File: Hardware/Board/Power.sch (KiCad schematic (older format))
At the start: 78 parts, among them Q100 2N7002, Q102 2N7002, Q103 2N7002, Q104 2N7002, U100 MAX17572, U101 MAX17572, U102 MAX17572, U104 MAX17574, U105 MAX17572

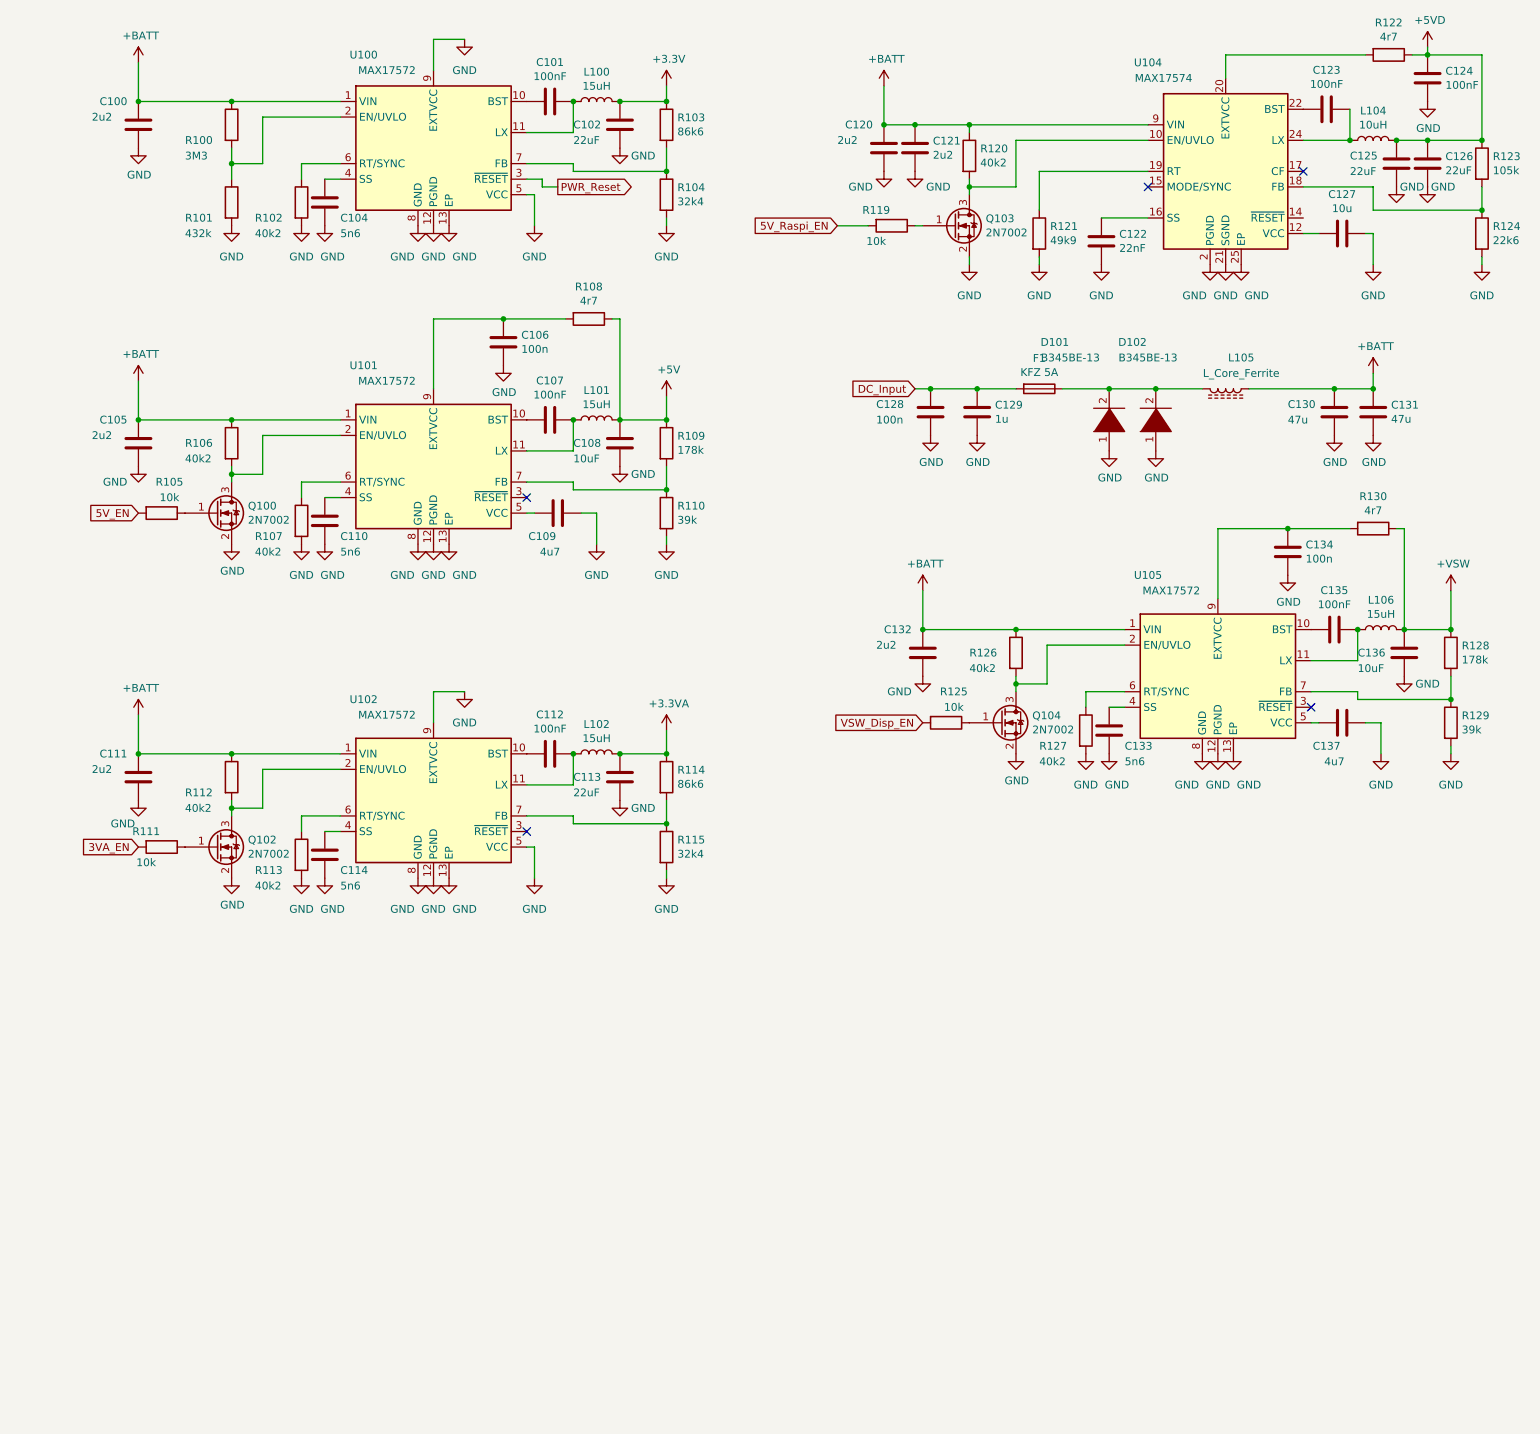
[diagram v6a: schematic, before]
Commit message: Display Unit Lib Fehler behoben, und noch Zeug raus geworfen Library jetzt projekt spezifisch im Hardware root.. Hauptplatine rund um den Prozessor a bissl was getan, vorbereitung Quadspi Flash und SD Karte.
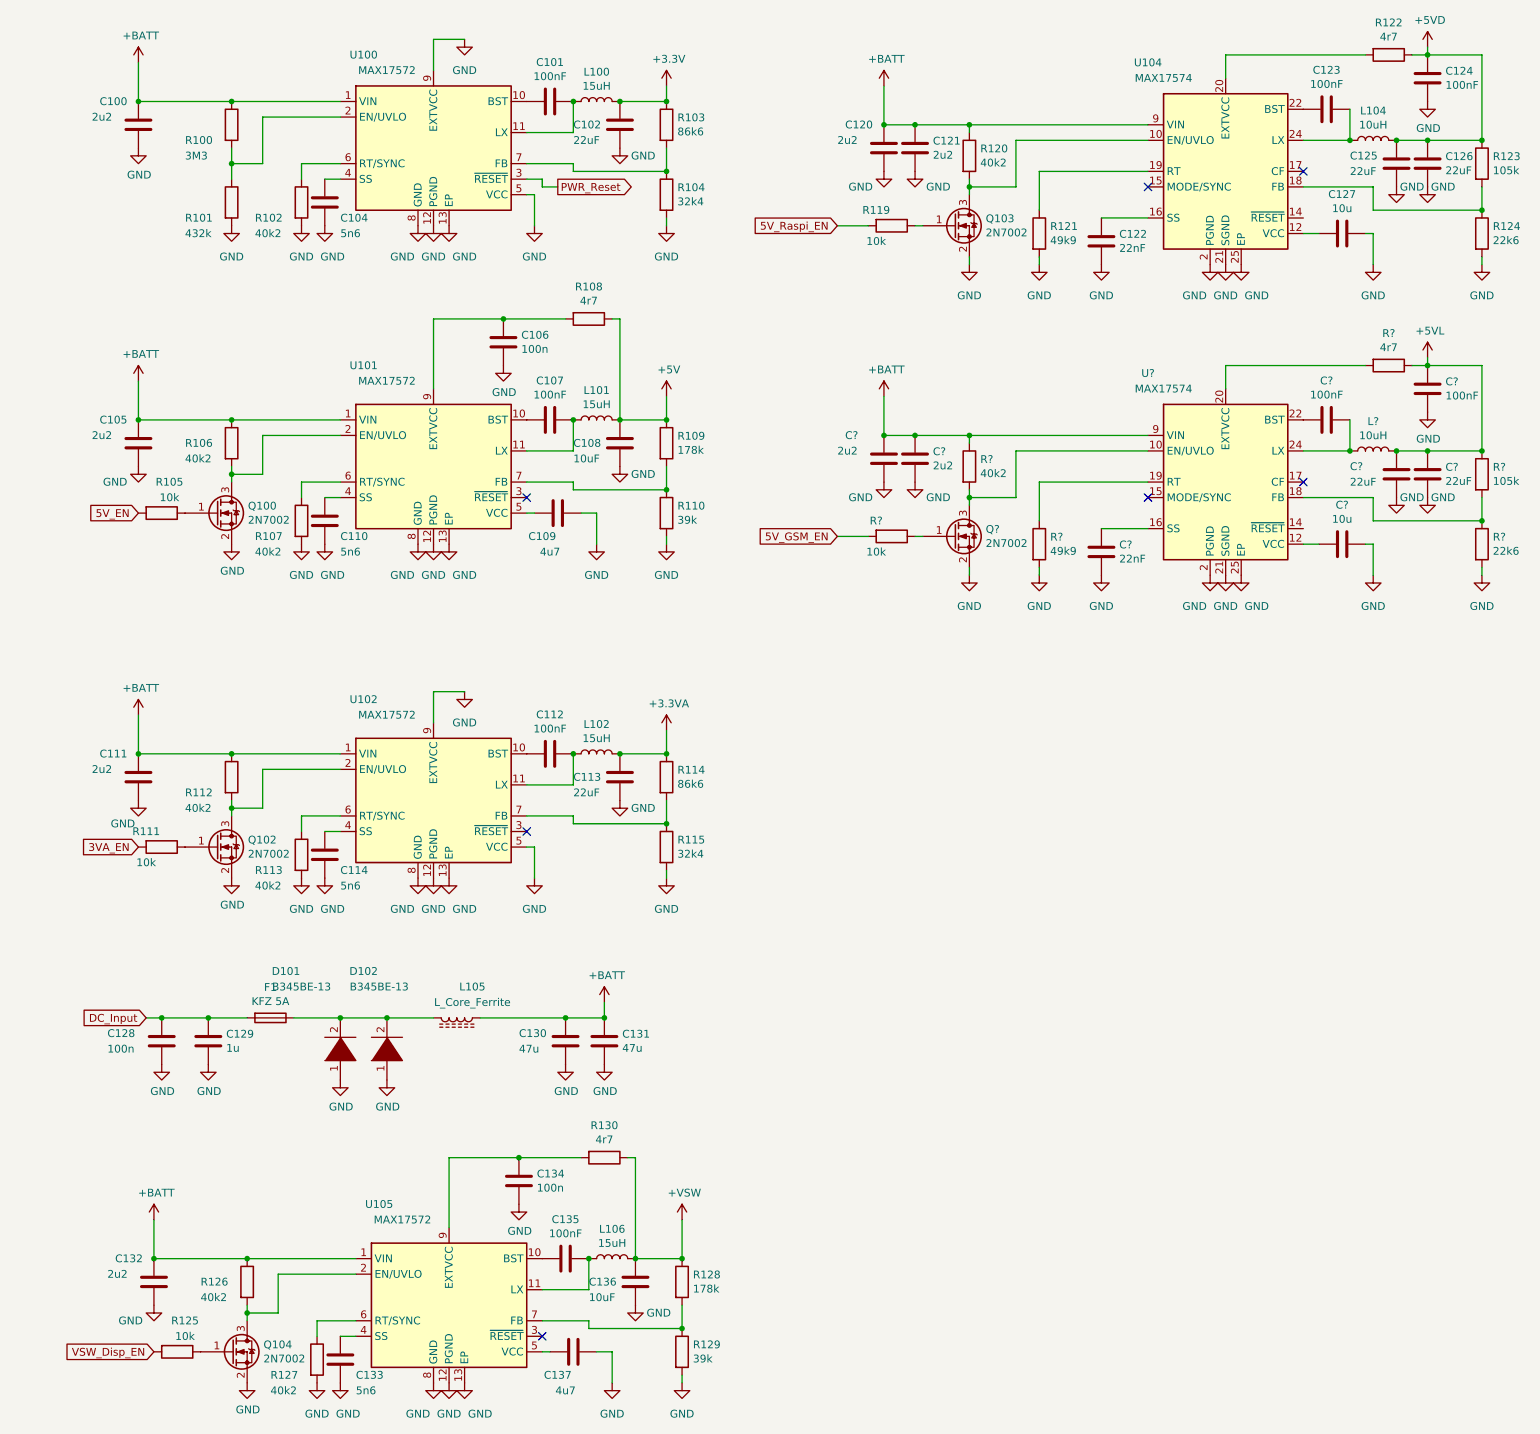
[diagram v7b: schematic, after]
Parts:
- added C?: 22nF, Capacitor_SMD:C_0603_1608Metric, symbol Device:C
- added C? (x2): 2u2, Capacitor_SMD:C_1210_3225Metric, symbol Device:C
- added C? (x2): 100nF, Capacitor_SMD:C_0603_1608Metric, symbol Device:C
- added C? (x2): 22uF, Capacitor_SMD:C_1210_3225Metric, symbol Device:C
- added C?: 10u, Capacitor_SMD:C_1210_3225Metric, symbol Device:C
- added L?: 10uH, SamacSys_Parts:XAL8080, symbol Device:L
- added Q?: 2N7002, Package_TO_SOT_SMD:SOT-23, symbol Transistor_FET:2N7002
- added R?: 105k, Resistor_SMD:R_0603_1608Metric, symbol Device:R
- added R?: 22k6, Resistor_SMD:R_0603_1608Metric, symbol Device:R
- added R?: 4r7, Resistor_SMD:R_0603_1608Metric, symbol Device:R
- added R?: 10k, Resistor_SMD:R_0603_1608Metric, symbol Device:R
- added R?: 40k2, Resistor_SMD:R_0603_1608Metric, symbol Device:R
- added R?: 49k9, Resistor_SMD:R_0603_1608Metric, symbol Device:R
- added U?: MAX17574, Package_DFN_QFN:QFN-24-1EP_4x5mm_P0.5mm_EP2.65x3.65mm, symbol Regulator_Switching:MAX17574
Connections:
- net +BATT: now also C?.1, C?.1, R?.1, U?.5 (VIN), U?.6 (VIN), U?.7 (VIN), U?.9 (VIN)
- net GND: now also C?.1, C?.2, C?.2, C?.2, C?.2, C?.2, C?.2, Q?.2 (S), R?.2, R?.2, U?.11 (PGND), U?.2 (PGND), U?.21 (SGND), U?.25 (EP), U?.3 (PGND)
- new net: C?.1, L?.1, U?.1 (LX), U?.23 (LX), U?.24 (LX)
- new net: Q?.3 (D), R?.2, U?.10 (EN/UVLO)
- new net: C?.2, U?.12 (VCC)
- new net: C?.1, U?.16 (SS)
- new net: R?.1, R?.2, U?.18 (FB)
- new net: R?.1, U?.19 (RT)
- new net: R?.2, U?.20 (EXTVCC)
- new net: C?.2, U?.22 (BST)
- new net: Q?.1 (G), R?.1
- new net +5VL: C?.1, C?.1, C?.1, L?.2, R?.1, R?.1
- new net 5V_GSM_EN: R?.2
- no-connect marks 5 -> 7
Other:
- moved on the sheet: C128, C129, C130, C131, C132, C133, C134, C135, C136, C137, D101, D102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

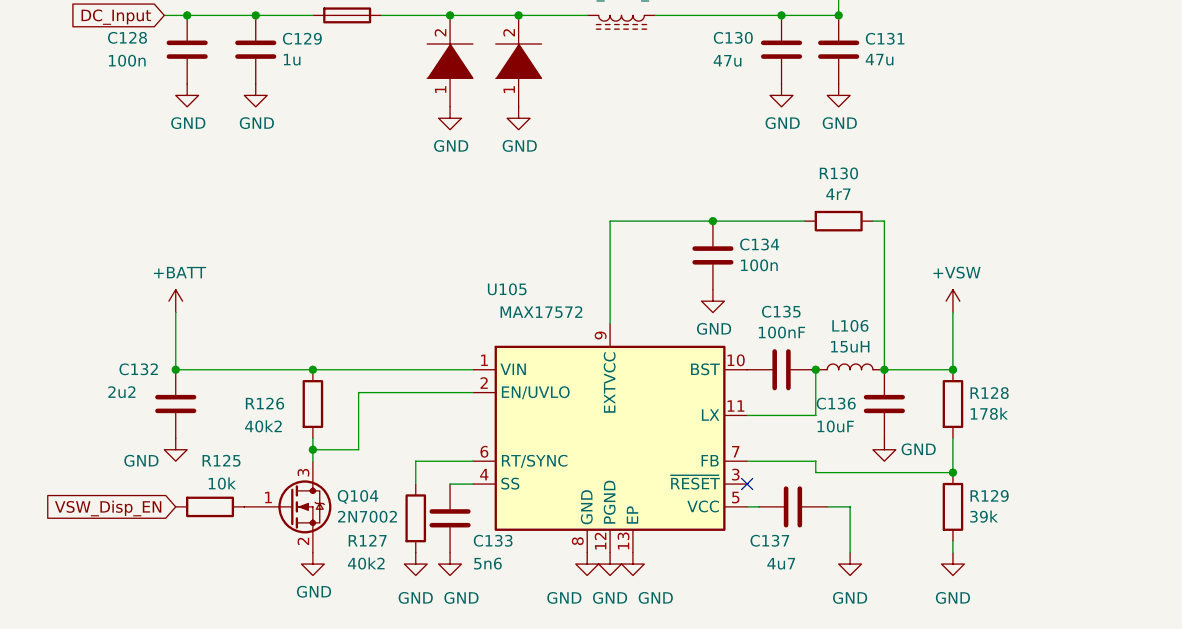
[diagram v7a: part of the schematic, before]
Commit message: Alle Busse aus dem Prozessor geroutet, Multplexing der LIN, RS485 und TTY Busse, diverse Aufräumarbeiten.
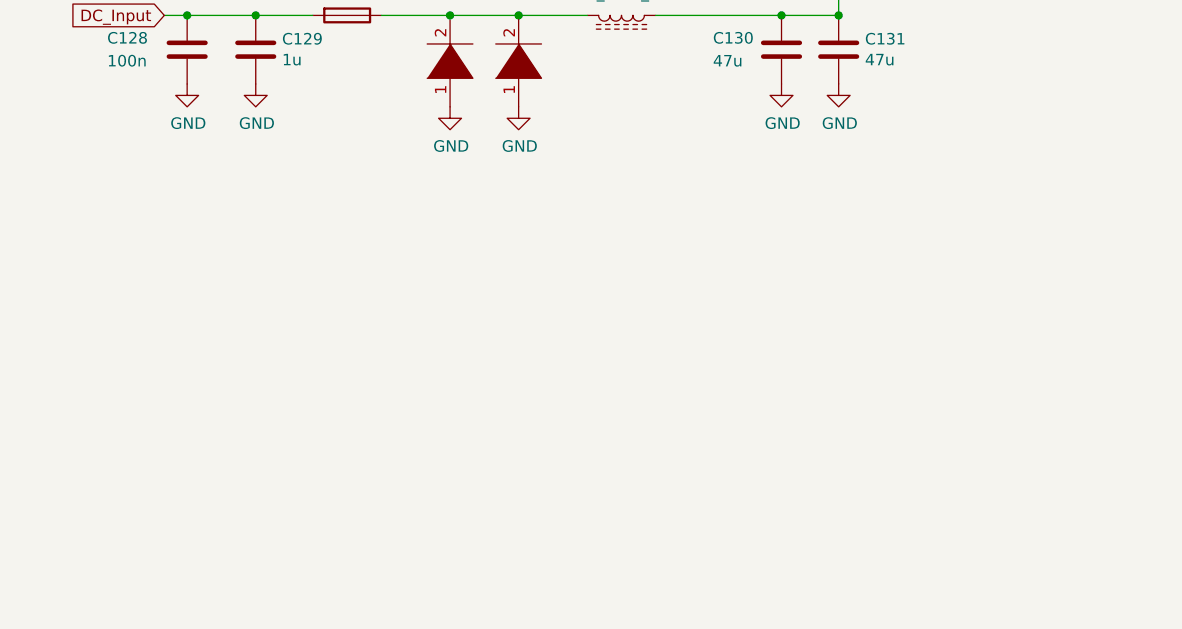
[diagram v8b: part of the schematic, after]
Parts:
- removed C132: 2u2, Capacitor_SMD:C_1210_3225Metric, symbol Device:C
- removed C133: 5n6, Capacitor_SMD:C_0603_1608Metric, symbol Device:C
- removed C134: 100n, Capacitor_SMD:C_0603_1608Metric, symbol Device:C
- removed C135: 100nF, Capacitor_SMD:C_0603_1608Metric, symbol Device:C
- removed C136: 10uF, Capacitor_SMD:C_1210_3225Metric, symbol Device:C
- removed C137: 4u7, Capacitor_SMD:C_1210_3225Metric, symbol Device:C
- removed L106: 15uH, Inductor_SMD:L_Coilcraft_XxL4040, symbol Device:L
- removed Q104: 2N7002, Package_TO_SOT_SMD:SOT-23, symbol Transistor_FET:2N7002
- removed R125: 10k, Resistor_SMD:R_0603_1608Metric, symbol Device:R
- removed R126, R127: 40k2, Resistor_SMD:R_0603_1608Metric, symbol Device:R
- removed R128: 178k, Resistor_SMD:R_0603_1608Metric, symbol Device:R
- removed R129: 39k, Resistor_SMD:R_0603_1608Metric, symbol Device:R
- removed R130: 4r7, Resistor_SMD:R_0603_1608Metric, symbol Device:R
- removed U105: MAX17572, Package_DFN_QFN:DFN-12-1EP_3x3mm_P0.5mm_EP2.05x2.86mm, symbol Regulator_Switching:MAX17572
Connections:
- no-connect marks 7 -> 6
